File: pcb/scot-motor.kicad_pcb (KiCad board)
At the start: 2 copper layers, 72 parts, among them IC1 MCP2562, IC2 STM32F0xxKxTx, J1 Conn_01x03_Female, J2 Conn_01x03_Female, J3 Conn_01x02_Female, J4 Conn_01x02_Female, J5 Conn_01x02_Female, J6 Conn_01x02_Female, J7 Conn_01x02_Female, J8 Conn_01x03_Male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

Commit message: pcb: Add brake clutch driver.
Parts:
- added D6: SS16HE, agg:SOD-323, F.Cu at (168.3, 52.8)
- added IC3: NCV8450A, Package_TO_SOT_SMD:SOT-223-3_TabPin2, F.Cu at (153.0, 45.7)
- added J9: Conn_01x02_Female, TerminalBlock_TE-Connectivity:TerminalBlock_TE_282834-2_1x02_P2.54mm_Horizontal, F.Cu at (169.4, 45.9)
- added Q1: BC817, Package_TO_SOT_SMD:SOT-23, F.Cu at (160.2, 46.8)
- added R20: 4K7, Resistor_SMD:R_0603_1608Metric_Pad1.05x0.95mm_HandSolder, F.Cu at (160.3, 43.1)
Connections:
- net /Power Supplies/POWER_28V+ renamed /MCU/POWER_28V+
- IC2 pad 26: Net-(IC2-Pad26) -> /MCU/nBRAKE

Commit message: pcb: Link brake clutch to e-stop, aesthetic tweaks.
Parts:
- added C24: 100n/3V3, Capacitor_SMD:C_0603_1608Metric_Pad1.05x0.95mm_HandSolder, F.Cu at (137.3, 51.9)
- added R21: 4K7, Resistor_SMD:R_0603_1608Metric_Pad1.05x0.95mm_HandSolder, F.Cu at (141.6, 51.9)
- added U10: 74AHC1G08, agg:SOT-23-5, F.Cu at (137.7, 48.4)
- R16, R17: value 330R -> 680R
- R20: value 4K7 -> 680R
- moved R20 18.4 mm to (142.5, 47.4)
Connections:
- C11 pad 1: VCC -> 3v3
- C12 pad 1: VCC -> 3v3
- C13 pad 1: VCC -> 3v3
- C15 pad 1: VCC -> 3v3
- C19 pad 1: VCC -> 3v3
- C20 pad 1: VCC -> 3v3
- C21 pad 1: VCC -> 3v3
- D5 pad 2: VCC -> 3v3
- FB2 pad 1: VCC -> 3v3
- R16 pad 1: /MCU/LIMIT_2_INPUT -> /MCU/LIMIT_1_INPUT
- R17 pad 1: /MCU/LIMIT_1_INPUT -> /MCU/LIMIT_2_INPUT
- R2 pad 1: /MCU/VI_I2C_SCL -> /MCU/VI_ALERT
- R20 pad 1: Net-(Q1-Pad1) -> /MCU/ESTOP_3V3
- R20 pad 2: /MCU/nBRAKE -> GND
- R3 pad 1: /MCU/VI_I2C_SDA -> /MCU/VI_I2C_SCL
- R5 pad 1: /MCU/VI_ALERT -> /MCU/VI_I2C_SDA
- U2 pad 1: /MCU/LIMIT_2_INPUT -> /MCU/LIMIT_1_INPUT
- U2 pad 10: /MCU/LIMIT_1_INPUT -> /MCU/LIMIT_2_INPUT
- U2 pad 11: /MCU/LIMIT_1 -> /MCU/LIMIT_2
- U2 pad 12: /MCU/LIMIT_1_INPUT -> /MCU/LIMIT_2_INPUT
- U2 pad 13: /MCU/LIMIT_1_INPUT -> /MCU/LIMIT_2_INPUT
- U2 pad 4: /MCU/LIMIT_2_INPUT -> /MCU/LIMIT_1_INPUT
- U2 pad 5: /MCU/LIMIT_2_INPUT -> /MCU/LIMIT_1_INPUT
- U2 pad 6: /MCU/LIMIT_2 -> /MCU/LIMIT_1
- U5 pad 5: VCC -> 3v3
- U7 pad 12: VCC -> 3v3
- U7 pad 14: VCC -> 3v3
- U7 pad 15: VCC -> 3v3
- U7 pad 16: VCC -> 3v3
- U8 pad 1: VCC -> 3v3
- U9 pad 1: VCC -> 3v3
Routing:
- net VCC: track 2.84 -> 0.00 mm, vias 4 -> 0
- net 3v3: track 3.50 -> 6.34 mm, vias 0 -> 4
- added copper zone on F.Cu, net 3v3
- removed copper zone on F.Cu, net VCC

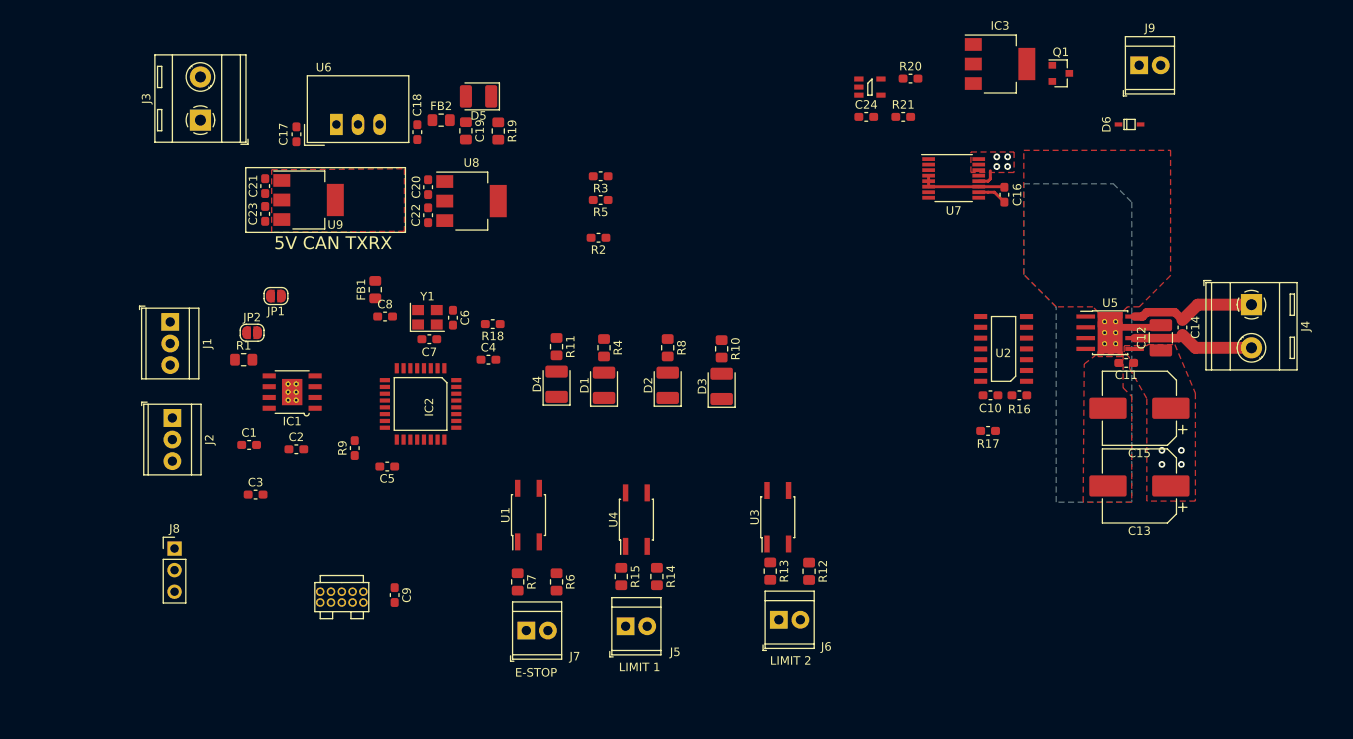
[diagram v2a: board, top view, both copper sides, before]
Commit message: PCB progress, schematic fixes.
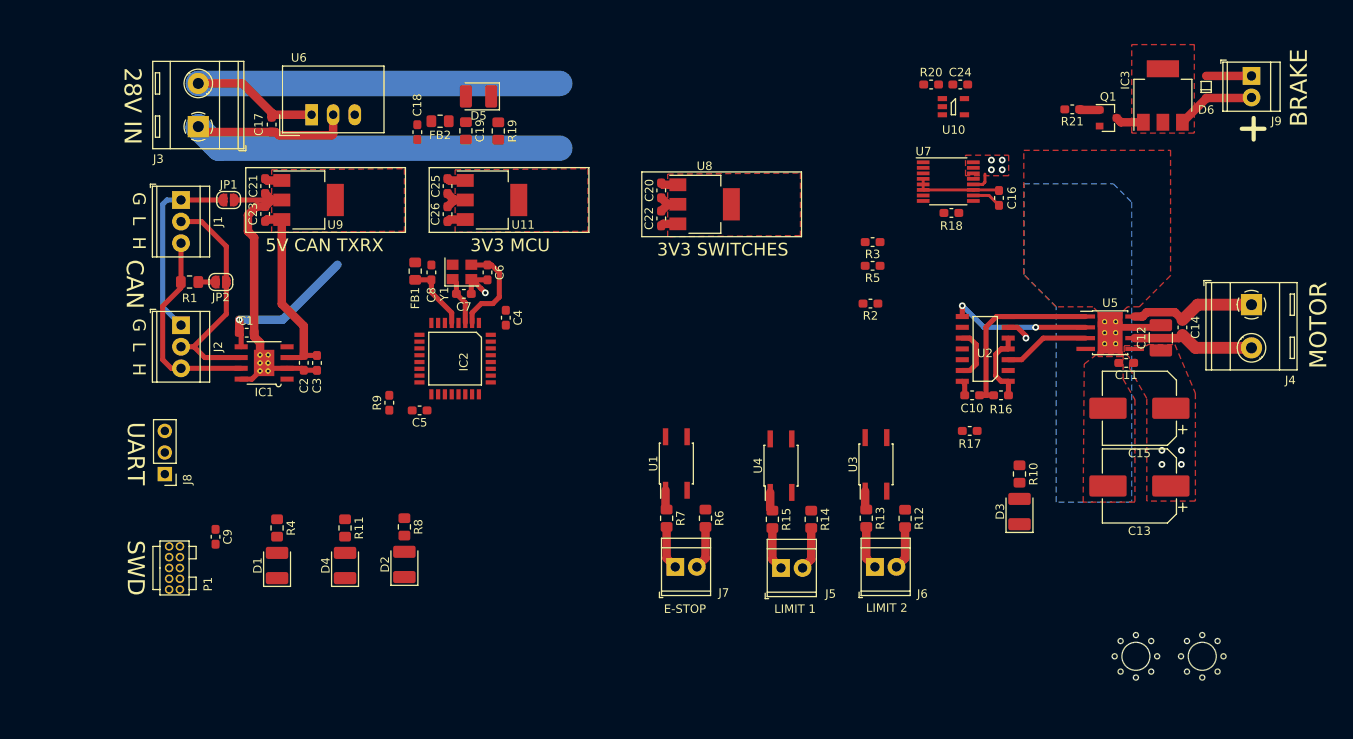
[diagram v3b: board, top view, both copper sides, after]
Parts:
- added C25: 1u/6.5V, Capacitor_SMD:C_0603_1608Metric_Pad1.05x0.95mm_HandSolder, F.Cu at (88.0, 60.1)
- added C26: 1u/3V3, Capacitor_SMD:C_0603_1608Metric_Pad1.05x0.95mm_HandSolder, F.Cu at (88.0, 63.4)
- added H1: MountingHole, agg:M3_MOUNT, F.Cu at (169.0, 115.4)
- added H2: MountingHole, agg:M3_MOUNT, F.Cu at (176.8, 115.4)
- added U11: MCP1703A-3302_SOT223, Package_TO_SOT_SMD:SOT-223-3_TabPin2, F.Cu at (93.2, 61.7)
- moved R18 55.5 mm to (147.3, 63.2), turned to 0 degrees
- moved D1 43.9 mm to (67.9, 104.7)
- moved R4 43.9 mm to (67.9, 100.3)
- moved D3 38.0 mm to (155.3, 98.4)
- moved R10 38.0 mm to (155.3, 94.0)
- moved D2 37.5 mm to (82.9, 104.6)
- moved R8 37.5 mm to (82.9, 100.2)
- moved R2 32.9 mm to (137.8, 73.9)
- moved R3 32.9 mm to (138.0, 66.7)
- moved R5 32.9 mm to (138.0, 69.5)
- moved D4 32.8 mm to (75.9, 104.7)
- moved R11 32.8 mm to (75.9, 100.3)
- moved C20 27.4 mm to (113.2, 60.6)
- moved C22 27.4 mm to (113.2, 63.9)
- moved U8 27.4 mm to (118.3, 62.2)
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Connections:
- C11 pad 1: 3v3 -> /Power Supplies/MOTOR_28V+
- C12 pad 1: 3v3 -> /Power Supplies/MOTOR_28V+
- C13 pad 1: 3v3 -> /Power Supplies/MOTOR_28V+
- C15 pad 1: 3v3 -> /Power Supplies/MOTOR_28V+
- C19 pad 1: 3v3 -> /Power Supplies/6V5_SWREG
- C20 pad 1: 3v3 -> /Power Supplies/6V5_SWREG
- C21 pad 1: 3v3 -> /Power Supplies/6V5_SWREG
- C22 pad 1: 3v3 -> +3.3VP
- C6 pad 2: Net-(C6-Pad2) -> GND
- C7 pad 2: Net-(C6-Pad2) -> GND
- D5 pad 2: 3v3 -> /Power Supplies/6V5_SWREG
- FB2 pad 1: 3v3 -> /Power Supplies/6V5_SWREG
- R12 pad 1: 3v3 -> +3.3VP
- R14 pad 1: 3v3 -> +3.3VP
- R6 pad 1: 3v3 -> +3.3VP
- U5 pad 5: 3v3 -> /Power Supplies/MOTOR_28V+
- U7 pad 12: 3v3 -> /Power Supplies/MOTOR_28V+
- U7 pad 14: 3v3 -> /Power Supplies/MOTOR_28V+
- U7 pad 15: 3v3 -> /Power Supplies/MOTOR_28V+
- U7 pad 16: 3v3 -> /Power Supplies/MOTOR_28V+
- U8 pad 1: 3v3 -> /Power Supplies/6V5_SWREG
- U8 pad 3: 3v3 -> +3.3VP
- U9 pad 1: 3v3 -> /Power Supplies/6V5_SWREG
- Y1 pad 2: Net-(C6-Pad2) -> GND
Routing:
- net GND: track 16.6 -> 161.4 mm, vias 0 -> 1
- net /MCU/POWER_28V+: track 0.00 -> 57.9 mm
- net /CAN Transceiver/CAN_L: track 0.00 -> 27.6 mm
- net /CAN Transceiver/CAN_H: track 0.00 -> 24.3 mm
- net Net-(J1-Pad1): track 0.00 -> 23.5 mm
- net /CAN Transceiver/5V_CAN: track 0.00 -> 22.7 mm
- net 3v3: track 6.34 -> 25.0 mm, vias 4 -> 1
- net Net-(U2-Pad8): track 0.00 -> 16.8 mm, vias 0 -> 2
- net Net-(C6-Pad1): track 0.00 -> 11.7 mm
- net Net-(U2-Pad3): track 0.00 -> 10.2 mm
- net /MCU/nBRAKE_DRIVE: track 0.00 -> 9.38 mm
- net /MCU/LIMIT_1_INPUT: track 0.00 -> 8.93 mm
- net Net-(C8-Pad1): track 0.00 -> 7.97 mm
- net /Power Supplies/6V5_SWREG: track 0.00 -> 6.26 mm
- net /MCU/LIMIT_2_INPUT: track 0.00 -> 6.22 mm
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- added copper zone on F.Cu, net /MCU/POWER_28V+
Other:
- board text added: "28V IN"
- board text added: "3V3 MCU"
- board text added: "3V3 SWITCHES"
- board text added: "BRAKE"
- board text added: "CAN"
- board text added: "G"
- board text added: "H"
- board text added: "L"
- board text added: "MOTOR"
- board text added: "SWD"
- board text added: "UART"

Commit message: PCB progress.
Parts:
- removed R18: 1K, Resistor_SMD:R_0603_1608Metric_Pad1.05x0.95mm_HandSolder
- R21: value 4K7 -> 1K
- moved H2 74.4 mm to (144.8, 48.3)
- moved R9 64.7 mm to (145.1, 95.5)
- moved C24 55.2 mm to (112.2, 89.9), turned to 180 degrees
- moved R20 51.0 mm to (115.7, 89.9), turned to 180 degrees
- moved U10 50.2 mm to (113.0, 87.3), turned to 180 degrees
- moved H1 25.1 mm to (144.1, 118.6)
- moved R3 22.8 mm to (115.9, 72.2)
- moved R5 22.5 mm to (115.9, 73.8)
- moved R2 22.1 mm to (115.9, 70.6)
- moved C17 21.6 mm to (88.8, 55.1), turned to 0 degrees
- moved C9 18.1 mm to (78.1, 106.6)
- moved J8 17.8 mm to (72.4, 96.7)
- moved FB1 17.7 mm to (101.9, 70.3)
- moved P1 17.4 mm to (72.5, 110.2)
- moved J3 16.2 mm to (74.9, 53.4)
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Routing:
- net GND: track 161.4 -> 476.8 mm, vias 1 -> 26
- net 3v3: track 25.0 -> 233.0 mm, vias 1 -> 4
- net /MCU/LIMIT_1: track 2.77 -> 74.9 mm, vias 1 -> 3
- net /MCU/LIMIT_2: track 0.00 -> 63.7 mm, vias 0 -> 3
- net /MCU/SWD_CLK: track 0.00 -> 63.4 mm, vias 0 -> 1
- net Net-(R21-Pad2): track 0.00 -> 63.1 mm, vias 0 -> 6
- net /MCU/SWD_IO: track 0.00 -> 56.7 mm, vias 0 -> 1
- net Net-(C9-Pad1): track 0.00 -> 56.2 mm, vias 0 -> 2
- net /MCU/VI_I2C_SCL: track 0.00 -> 55.0 mm, vias 0 -> 2
- net /Power Supplies/6V5_SWREG: track 6.26 -> 59.0 mm
- net /MCU/VI_ALERT: track 0.00 -> 51.8 mm, vias 0 -> 1
- net /MCU/VI_I2C_SDA: track 0.00 -> 48.2 mm, vias 0 -> 2
- net /MCU/PWM_CH1: track 0.00 -> 44.5 mm, vias 0 -> 2
- net /Power Supplies/MOTOR_28V+: track 2.84 -> 45.3 mm, vias 4 -> 10
- net /MCU/POWER_28V+: track 57.9 -> 98.7 mm, vias 0 -> 4
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- added copper zone on F.Cu, net /Power Supplies/MOTOR_28V+
- removed copper zone on F.Cu, net 3v3
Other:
- board outline added: 142.7 x 57.9 mm
- board text added: "6.5VDC OK"

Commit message: PCB Progress.
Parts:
- C17: value 2u2/35V -> 4u7/35V; footprint Capacitor_SMD:C_0603_1608Metric_Pad1.05x0.95mm_HandSolder -> Capacitor_SMD:C_1206_3216Metric_Pad1.42x1.75mm_HandSolder
- moved D3 14.2 mm to (145.2, 105.9), turned to 270 degrees
- moved J6 12.4 mm to (119.8, 115.7)
- moved U4 11.1 mm to (132.0, 101.1)
- moved R15 11.1 mm to (131.0, 107.6)
- moved R14 11.1 mm to (135.6, 107.6)
- moved U3 11.1 mm to (121.0, 101.1)
- moved R12 11.1 mm to (124.4, 107.6)
- moved R13 11.1 mm to (119.8, 107.6)
- moved J5 10.4 mm to (131.0, 115.7)
- moved R9 4.87 mm to (142.4, 91.4), turned to 0 degrees
- moved R11 2.95 mm to (92.1, 97.7)
- moved R4 2.95 mm to (84.1, 97.7)
- moved R8 2.95 mm to (99.1, 97.5)
- moved D6 2.74 mm to (167.3, 52.0)
- moved J9 2.74 mm to (172.6, 50.7)
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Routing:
- net +3.3VP: track 30.4 -> 82.7 mm, vias 3 -> 4
- net /MCU/nFAULT: track 39.0 -> 80.9 mm
- net GND: track 476.8 -> 517.9 mm, vias 26 -> 33
- net /MCU/LIMIT_2_INPUT: track 6.22 -> 38.7 mm, vias 0 -> 2
- net /MCU/LIMIT_1_INPUT: track 8.93 -> 26.0 mm
- net Net-(D3-Pad2): track 0.00 -> 15.3 mm
- net 3v3: track 233.0 -> 246.6 mm, vias 4 -> 7
- net /MCU/ESTOP_3V3: track 26.8 -> 39.0 mm, vias 0 -> 2
- net /MCU/LIMIT_1: track 74.9 -> 72.0 mm
- net /MCU/LIMIT_2: track 63.7 -> 60.7 mm
- net /MCU/CONTROL_OK: track 28.3 -> 25.3 mm
- net /MCU/LIMIT_2A: track 5.10 -> 7.98 mm
- net /MCU/ESTOP_A: track 5.12 -> 7.98 mm
- net /MCU/LIMIT_1A: track 5.12 -> 7.98 mm
- net Net-(R21-Pad2): track 63.1 -> 65.4 mm
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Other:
- board size 142.7 x 57.9 mm -> 115.1 x 80.1 mm
- board text added: "A"
- board text added: "April 2020"
- board text added: "B"
- board text added: "CONTROL"
- board text added: "Clutch Driver"
- board text added: "Ground"
- board text added: "Interlock Logic"
- board text added: "MOTOR FAULT"
- board text added: "Phil M0DNY"
- board text added: "R"
- board text added: "SCOT Motor I/F"
- board text added: "Switch Isolation"
- board text added: "T"
- board text added: "Termination"
- board text added: "V/I Monitoring"

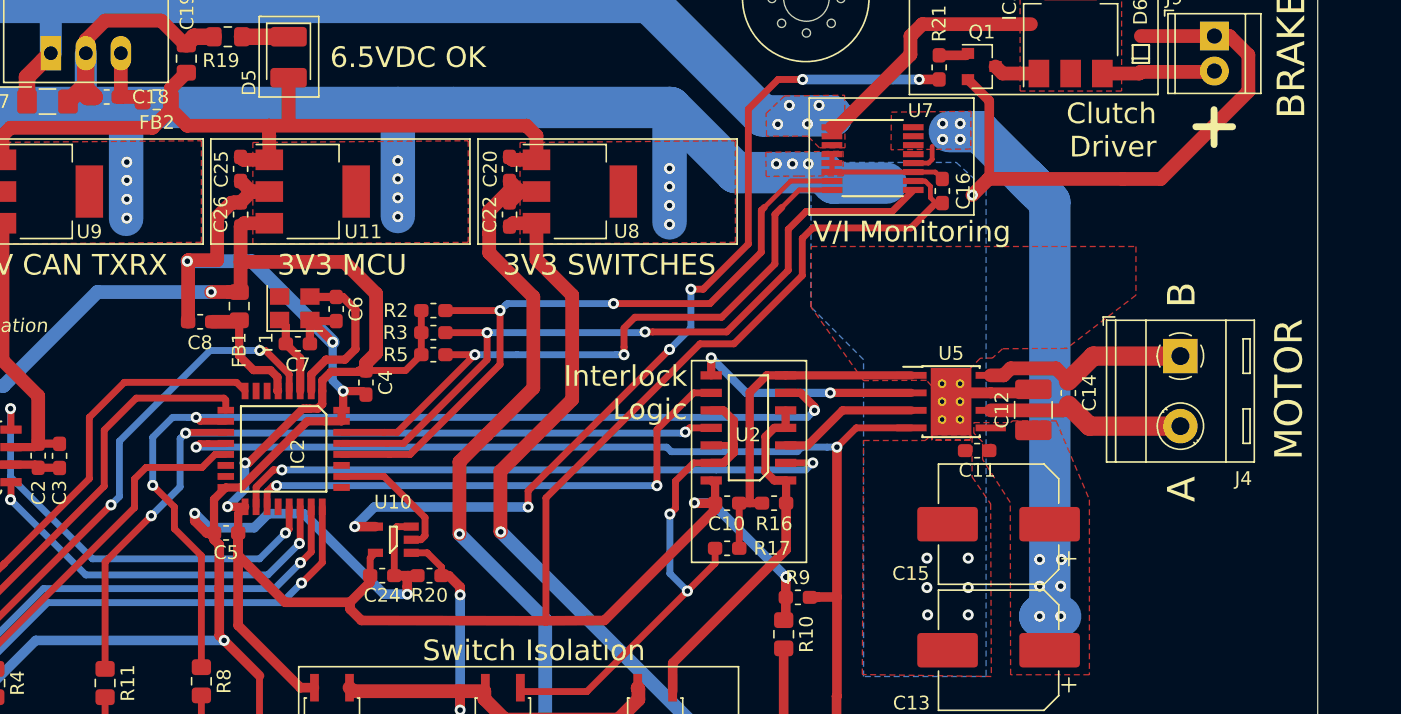
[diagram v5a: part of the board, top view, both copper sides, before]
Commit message: pcb: Add ground terminal on motor terminal block for shielding.
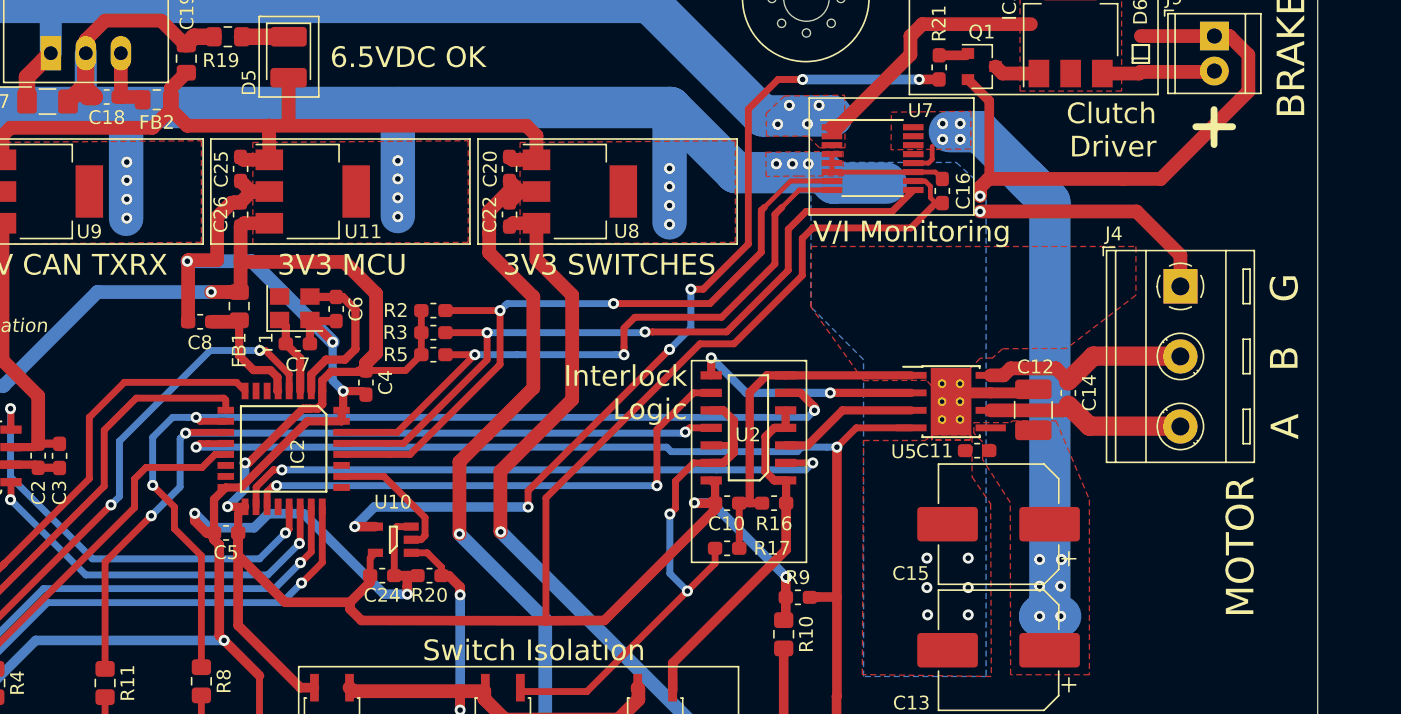
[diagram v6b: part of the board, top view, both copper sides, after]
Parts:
- C17: value 4u7/35V -> 4u7/50V
- J4: value Conn_01x02_Female -> Conn_01x03_Female; footprint TerminalBlock_RND:TerminalBlock_RND_205-00287_1x02_P5.08mm_Horizontal -> TerminalBlock_RND:TerminalBlock_RND_205-00288_1x03_P5.08mm_Horizontal
- moved J4 5.05 mm to (170.1, 68.9)
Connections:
- J4 pad 1: /MCU/MOTOR_B -> GND
- J4 pad 2: /MCU/MOTOR_A -> /MCU/MOTOR_B
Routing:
- net GND: track 517.9 -> 535.9 mm, vias 33 -> 34
